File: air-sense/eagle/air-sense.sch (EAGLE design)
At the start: 6 parts

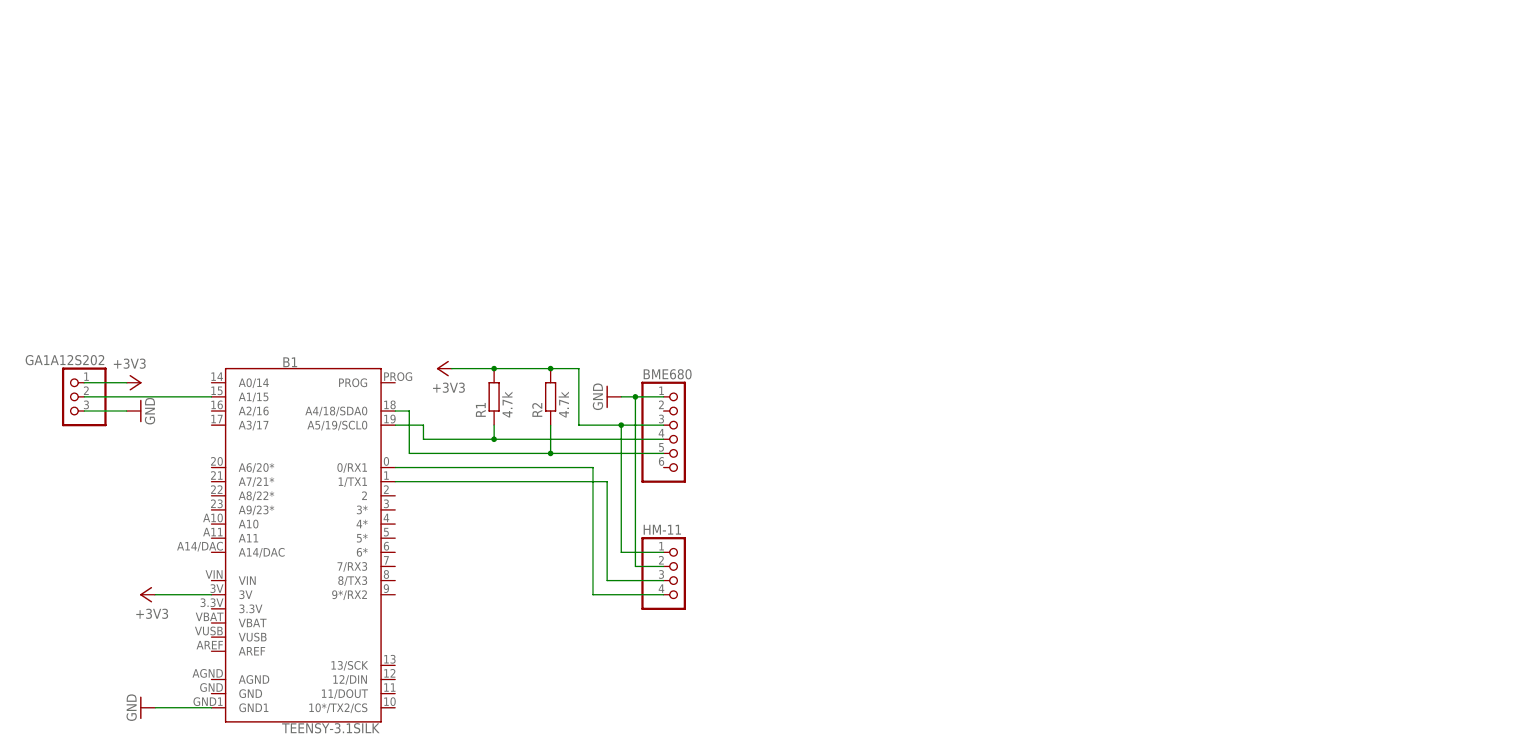
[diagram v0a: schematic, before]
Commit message: Add air-sense v2 eagle files with hm-11 pads
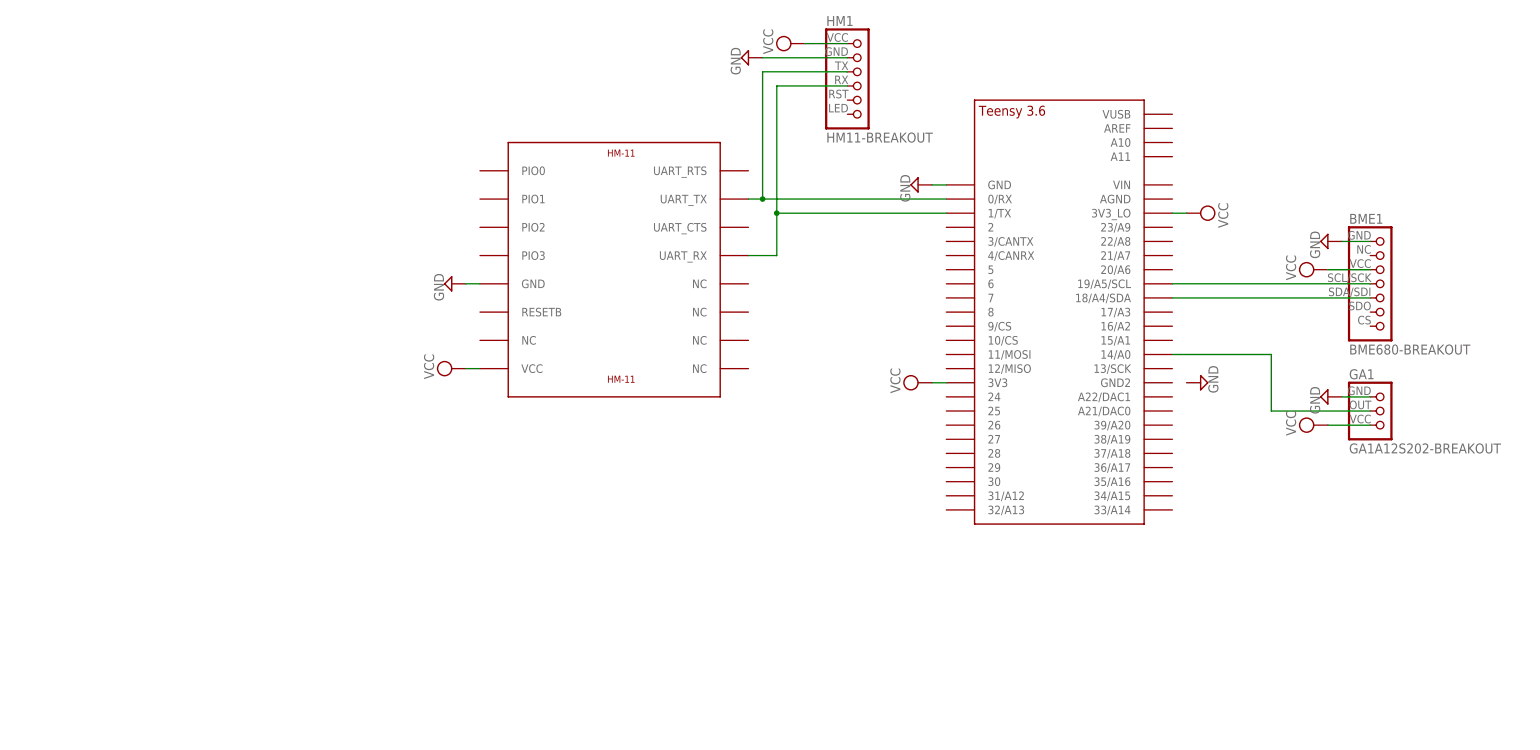
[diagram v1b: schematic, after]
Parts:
- removed B1: TEENSY-3.1SILK, SparkFun-Boards:TEENSY-3.1SILK
- removed BME680: (no value), pinhead:PINHD-1X6
- removed GA1A12S202: (no value), pinhead:PINHD-1X3
- removed HM-11: (no value), pinhead:PINHD-1X4
- removed R1, R2: 4.7k, resistor:R-EU_R2012
- added BME1: BME680-BREAKOUT, AQ-Parts:BME680-BREAKOUT
- added GA1: GA1A12S202-BREAKOUT, AQ-Parts:GA1A12S202-BREAKOUT
- added HM1: HM11-BREAKOUT, AQ-Parts:HM11-BREAKOUT
- added U$1: TEENSY_3.5/3.6_BASIC, Teensy356:TEENSY_3.5/3.6_BASIC
- added U$2: HM-11, smartwatch-hm11:HM-11
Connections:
- removed net +3V3: B1.3V, BME680.3, GA1A12S202.1, HM-11.1, R1.2, R2.2
- removed net N$4: B1.1/TX1, HM-11.3
- removed net N$5: B1.0/RX1, HM-11.4
- new net SCL: BME1.SCL/SCK, U$1.19/A5/SCL
- new net SDA: BME1.SDA/SDI, U$1.18/A4/SDA
- new net VCC: BME1.VCC, GA1.VCC, HM1.VCC, U$1.3V3, U$1.3V3_LO, U$2.VCC
- net GND: now also BME1.GND, GA1.GND, HM1.GND, U$1.GND, U$2.GND; no longer B1.GND1, BME680.1, GA1A12S202.3, HM-11.2
- net N$1: now also HM1.TX, U$1.0/RX, U$2.UART_TX; no longer B1.A4/18/SDA0, BME680.5, R2.1
- net N$2: now also HM1.RX, U$1.1/TX, U$2.UART_RX; no longer B1.A5/19/SCL0, BME680.4, R1.1
- net N$3: now also GA1.OUT, U$1.14/A0; no longer B1.A1/15, GA1A12S202.2
